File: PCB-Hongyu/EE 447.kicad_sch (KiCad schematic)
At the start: 9 parts, among them J1 Conn_01x04_Pin, U1 TSC2046IPWR

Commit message: file
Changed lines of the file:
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@@
 	)
 	(sheet
-		(at 203.2 26.67)
-		(size 22.86 29.21)
+		(at 217.17 26.67)
+		(size 20.32 21.59)
 		(exclude_from_sim no)
 		(in_bom yes)
@@
 		)
 		(property "Sheetname" "Epaper"
-			(at 203.2 25.9584 0)
+			(at 217.17 25.9584 0)
 			(effects
 				(font
@@
 		)
 		(property "Sheetfile" "../PCB_June/PCB.kicad_sch"
-			(at 203.2 56.4646 0)
+			(at 217.17 48.8446 0)
 			(effects
 				(font

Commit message: yur
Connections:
- net EPD_DC: now reaches U2.25 (IO5)
- net EPD_RST: now reaches U2.26 (IO4)
- net EPD_BUSY: now reaches U2.28 (IO18)
- net EPD_CS: now reaches U2.5 (IO3)
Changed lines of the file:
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@@
+	(wire
+		(pts
+			(xy 154.94 83.82) (xy 161.29 83.82)
+		)
+		(stroke
+			(width 0)
+			(type default)
+		)
+	)
 	(wire
 		(pts
@@
 	(wire
 		(pts
+			(xy 154.94 78.74) (xy 161.29 78.74)
+		)
+		(stroke
+			(width 0)
+			(type default)
+		)
+	)
+	(wire
+		(pts
 			(xy 80.01 95.25) (xy 80.01 96.52)
 		)
@@
 	(wire
 		(pts
+			(xy 124.46 63.5) (xy 130.81 63.5)
+		)
+		(stroke
+			(width 0)
+			(type default)
+		)
+	)
+	(wire
+		(pts
 			(xy 77.47 119.38) (xy 77.47 110.49)
 		)
@@
 		(pts
 			(xy 77.47 110.49) (xy 110.49 110.49)
+		)
+		(stroke
+			(width 0)
+			(type default)
+		)
+	)
+	(wire
+		(pts
+			(xy 154.94 76.2) (xy 161.29 76.2)
 		)
 		(stroke
@@
 		)
 	)
+	(global_label "EPD_DC"
+		(shape output)
+		(at 161.29 76.2 0)
+		(fields_autoplaced yes)
+		(effects
+			(font
+				(size 1.27 1.27)
+			)
+			(justify left)
+		)
+		(property "Intersheetrefs" "${INTERSHEET_REFS}"
+			(at 171.4718 76.2 0)
+			(effects
+				(font
+					(size 1.27 1.27)
+				)
+				(justify left)
+				(hide yes)
+			)
+		)
+	)
 	(global_label "CLK"
 		(shape input)
@@
 		)
 	)
+	(global_label "EPD_CS"
+		(shape output)
+		(at 124.46 63.5 180)
+		(fields_autoplaced yes)
+		(effects
+			(font
+				(size 1.27 1.27)
+			)
+			(justify right)
+		)
+		(property "Intersheetrefs" "${INTERSHEET_REFS}"
+			(at 114.3387 63.5 0)
+			(effects
+				(font
+					(size 1.27 1.27)
+				)
+				(justify right)
+				(hide yes)
+			)
+		)
+	)
 	(global_label "CS_TSC"
 		(shape input)
@@
 			(effects
 				(font
+					(size 1.27 1.27)
+				)
+				(justify left)
+				(hide yes)
+			)
+		)
+	)
+	(global_label "EPD_RST"
+		(shape output)
+		(at 161.29 78.74 0)
+		(fields_autoplaced yes)
+		(effects
+			(font
+				(size 1.27 1.27)
+			)
+			(justify left)
+		)
+		(property "Intersheetrefs" "${INTERSHEET_REFS}"
+			(at 172.3789 78.74 0)
+			(effects
+				(font
+					(size 1.27 1.27)
+				)
+				(justify left)
+				(hide yes)
+			)
+		)
+	)
+	(global_label "EPD_BUSY"
+		(shape output)
+		(at 161.29 83.82 0)
+		(fields_autoplaced yes)
+		(effects
+			(font
+				(size 1.27 1.27)
+			)
+			(justify left)
+		)
+		(property "Intersheetrefs" "${INTERSHEET_REFS}"
+			(at 173.8304 83.82 0)
+			(effects
+				(font

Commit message: MCB
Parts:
- added H1, H2, H3: MountingHole, MountingHole:MountingHole_3.2mm_M3, symbol Mechanical:MountingHole
- C1, C2, C3, C5: value ~ -> NC
- C4: value 10 uF -> 10u
- C6: value 0.1 uF -> 0.1u
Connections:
- net PENIRQ: now reaches U2.20 (IO9)
- net PENIRQ: now also U1.11 (*PENIRQ)
- no-connect marks 2 -> 8

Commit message: added power digikey links
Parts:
- C1, C2, C3, C5: now not fitted
- C4: Part Number (none) -> GRM21BR61H106KE43L
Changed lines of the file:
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@@
 			)
 		)
-		(property "Datasheet" "~"
+		(property "Datasheet" "https://www.digikey.com/en/products/detail/murata-electronics/GRM21BR61H106KE43L/10326316"
 			(at 80.01 91.44 0)
 			(effects
@@
 			)
 		)
+		(property "Part Number" "GRM21BR61H106KE43L"
+			(at 80.01 91.44 0)
+			(effects
+				(font
+					(size 1.27 1.27)
+				)
+				(hide yes)
+			)
+		)
 		(pin "1"
 		)
@@
 		(in_bom yes)
 		(on_board yes)
-		(dnp no)
+		(dnp yes)
 		(fields_autoplaced yes)
 		(property "Reference" "C2"
@@
 		(in_bom yes)
 		(on_board yes)
-		(dnp no)
+		(dnp yes)
 		(fields_autoplaced yes)
 		(property "Reference" "C3"
@@
 		(in_bom yes)
 		(on_board yes)
-		(dnp no)
+		(dnp yes)
 		(fields_autoplaced yes)
 		(property "Reference" "C5"
@@
 		(in_bom yes)
 		(on_board yes)
-		(dnp no)
+		(dnp yes)
 		(fields_autoplaced yes)
 		(property "Reference" "C1"

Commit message: added some stuff
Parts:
- C1, C2, C3, C5: footprint Capacitor_SMD:C_0805_2012Metric_Pad1.18x1.45mm_HandSolder -> Capacitor_SMD:C_0603_1608Metric_Pad1.08x0.95mm_HandSolder; now fitted
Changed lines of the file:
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@@
 		(in_bom yes)
 		(on_board yes)
-		(dnp yes)
+		(dnp no)
 		(fields_autoplaced yes)
 		(property "Reference" "C2"
@@
 			)
 		)
-		(property "Footprint" "Capacitor_SMD:C_0805_2012Metric_Pad1.18x1.45mm_HandSolder"
+		(property "Footprint" "Capacitor_SMD:C_0603_1608Metric_Pad1.08x0.95mm_HandSolder"
 			(at 65.7352 127 0)
 			(effects
@@
 			)
 		)
-		(property "Datasheet" "~"
+		(property "Datasheet" "https://www.digikey.com/en/products/detail/samsung-electro-mechanics/CL21B104KBCNNNC/3886661"
 			(at 93.98 91.44 0)
 			(effects
@@
 		(in_bom yes)
 		(on_board yes)
-		(dnp yes)
+		(dnp no)
 		(fields_autoplaced yes)
 		(property "Reference" "C3"
@@
 			)
 		)
-		(property "Footprint" "Capacitor_SMD:C_0805_2012Metric_Pad1.18x1.45mm_HandSolder"
+		(property "Footprint" "Capacitor_SMD:C_0603_1608Metric_Pad1.08x0.95mm_HandSolder"
 			(at 78.4352 127 0)
 			(effects
@@
 		(in_bom yes)
 		(on_board yes)
-		(dnp yes)
+		(dnp no)
 		(fields_autoplaced yes)
 		(property "Reference" "C5"
@@
 			)
 		)
-		(property "Footprint" "Capacitor_SMD:C_0805_2012Metric_Pad1.18x1.45mm_HandSolder"
+		(property "Footprint" "Capacitor_SMD:C_0603_1608Metric_Pad1.08x0.95mm_HandSolder"
 			(at 91.1352 127 0)
 			(effects
@@
 		(in_bom yes)
 		(on_board yes)
-		(dnp yes)
+		(dnp no)
 		(fields_autoplaced yes)
 		(property "Reference" "C1"
@@
 			)
 		)
-		(property "Footprint" "Capacitor_SMD:C_0805_2012Metric_Pad1.18x1.45mm_HandSolder"
+		(property "Footprint" "Capacitor_SMD:C_0603_1608Metric_Pad1.08x0.95mm_HandSolder"
 			(at 53.0352 127 0)
 			(effects

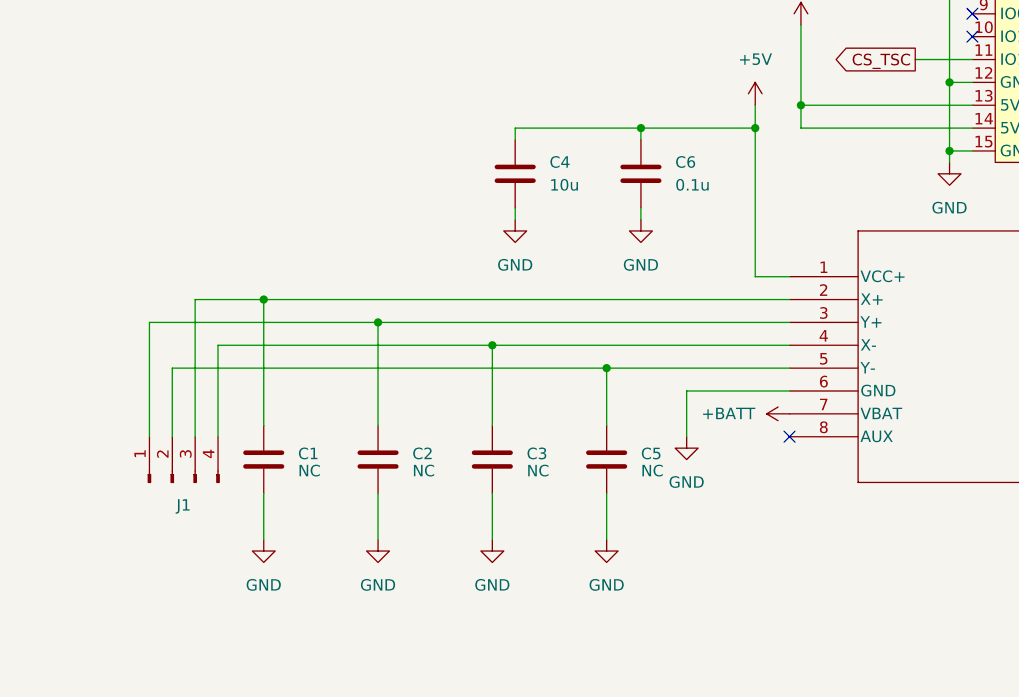
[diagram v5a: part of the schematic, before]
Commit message: finished adding parts and fixing silkscreen
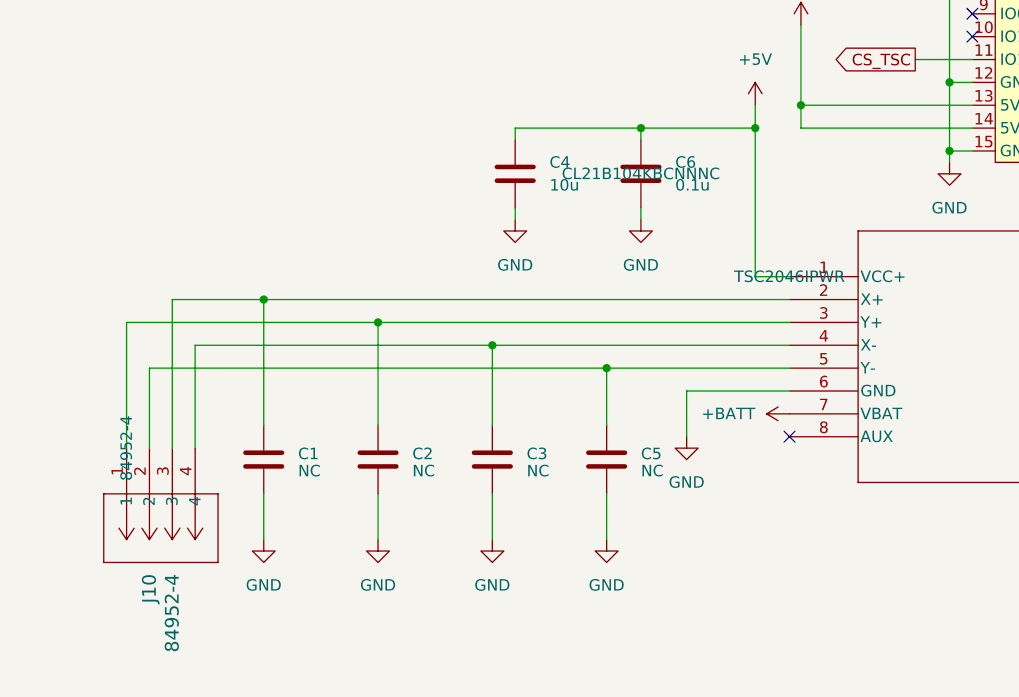
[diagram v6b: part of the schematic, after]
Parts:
- removed J1: Conn_01x04_Pin, Connector_FFC-FPC:JUSHUO_AFA07-S04FCA-00_1x4-1MP_P1.0mm_Horizontal, symbol Connector:Conn_01x04_Pin
- added J10: 84952-4, Hongyu:CON4_SMT-RA_FCC-FPC2, symbol 2025-04-15_05-15-59:84952-4
- C6: Part Number (none) -> CL21B104KBCNNNC
- U1: Part Number (none) -> TSC2046IPWR
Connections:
- net at C2.1, U1.3 (Y+): now also J10.1
- net at C5.1, U1.5 (Y-): now also J10.2
- net at C1.1, U1.2 (X+): now also J10.3
- net at C3.1, U1.4 (X-): now also J10.4
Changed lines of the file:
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@@
 	(wire
 		(pts
-			(xy 44.45 105.41) (xy 44.45 120.65)
+			(xy 39.37 113.03) (xy 39.37 121.92)
 		)
 		(stroke
@@
 	(wire
 		(pts
-			(xy 46.99 110.49) (xy 77.47 110.49)
+			(xy 44.45 110.49) (xy 77.47 110.49)
 		)
 		(stroke
@@
 	(wire
 		(pts
-			(xy 39.37 107.95) (xy 39.37 120.65)
-		)
-		(stroke
-			(width 0)
-			(type default)
-		)
-	)
-	(wire
-		(pts
 			(xy 111.76 83.82) (xy 130.81 83.82)
 		)
@@
 	(wire
 		(pts
-			(xy 44.45 105.41) (xy 52.07 105.41)
-		)
-		(stroke
-			(width 0)
-			(type default)
-		)
-	)
-	(wire
-		(pts
-			(xy 41.91 113.03) (xy 90.17 113.03)
-		)
-		(stroke
-			(width 0)
-			(type default)
-		)
-	)
-	(wire
-		(pts
-			(xy 41.91 113.03) (xy 41.91 120.65)
+			(xy 41.91 105.41) (xy 52.07 105.41)
+		)
+		(stroke
+			(width 0)
+			(type default)
+		)
+	)
+	(wire
+		(pts
+			(xy 39.37 113.03) (xy 90.17 113.03)
 		)
 		(stroke
@@
 	(wire
 		(pts
-			(xy 46.99 110.49) (xy 46.99 120.65)
-		)
-		(stroke
-			(width 0)
-			(type default)
-		)
-	)
-	(wire
-		(pts
 			(xy 90.17 113.03) (xy 110.49 113.03)
 		)
@@
 	(wire
 		(pts
-			(xy 39.37 107.95) (xy 64.77 107.95)
+			(xy 36.83 107.95) (xy 64.77 107.95)
 		)
 		(stroke
@@
 	(wire
 		(pts
+			(xy 41.91 105.41) (xy 41.91 121.92)
+		)
+		(stroke
+			(width 0)
+			(type default)
+		)
+	)
+	(wire
+		(pts
 			(xy 106.68 83.82) (xy 106.68 86.36)
 		)
@@
 	(wire
 		(pts
+			(xy 44.45 110.49) (xy 44.45 121.92)
+		)
+		(stroke
+			(width 0)
+			(type default)
+		)
+	)
+	(wire
+		(pts
 			(xy 163.83 58.42) (xy 163.83 55.88)
 		)
@@
 		(pts
 			(xy 128.27 71.12) (xy 128.27 81.28)
+		)
+		(stroke
+			(width 0)
+			(type default)
+		)
+	)
+	(wire
+		(pts
+			(xy 36.83 107.95) (xy 36.83 121.92)
 		)
 		(stroke
@@
 	)
 	(symbol
+		(lib_id "2025-04-15_05-15-59:84952-4")
+		(at 36.83 121.92 90)
+		(mirror x)
+		(unit 1)
+		(exclude_from_sim no)
+		(in_bom yes)
+		(on_board yes)
+		(dnp no)
+		(property "Reference" "J10"
+			(at 39.3699 135.89 0)
+			(effects
+				(font
+					(size 1.524 1.524)
+				)
+				(justify left)
+			)
+		)
+		(property "Value" "84952-4"
+			(at 41.9099 135.89 0)
+			(effects
+				(font
+					(size 1.524 1.524)
+				)
+				(justify left)
+			)
+		)
+		(property "Footprint" "Hongyu:CON4_SMT-RA_FCC-FPC2"
+			(at 36.83 121.92 0)
+			(effects
+				(font
+					(size 1.27 1.27)
+					(italic yes)
+				)
+				(hide yes)
+			)
+		)
+		(property "Datasheet" "https://www.digikey.com/en/products/detail/te-connectivity-amp-connectors/84952-4/2056112"
+			(at 36.83 121.92 0)
+			(effects
+				(font
+					(size 1.27 1.27)
+					(italic yes)
+				)
+				(hide yes)
+			)
+		)
+		(property "Description" ""
+			(at 36.83 121.92 0)
+			(effects
+				(font
+					(size 1.27 1.27)
+				)
+				(hide yes)
+			)
+		)
+		(property "Part Number" "84952-4"
+			(at 36.83 121.92 0)
+			(effects
+				(font
+					(size 1.27 1.27)
+				)
+			)
+		)
+		(pin "3"
+		)
+		(pin "1"
+		)
+		(pin "2"
+		)
+		(pin "4"
+		)
+		(instances
+			(project ""
+				(path "/8dcae476-bf02-4dea-8567-670805b7ab7c"
+					(reference "J10")
+					(unit 1)
+				)
+			)
+		)
+	)
+	(symbol
 		(lib_id "power:+BATT")
 		(at 111.76 74.93 0)
@@
 	)
 	(symbol
-		(lib_id "Connector:Conn_01x04_Pin")
-		(at 41.91 125.73 90)
-		(unit 1)
-		(exclude_from_sim no)
-		(in_bom yes)
-		(on_board yes)
-		(dnp no)
-		(fields_autoplaced yes)
-		(property "Reference" "J1"
-			(at 43.18 128.27 90)
-			(effects
-				(font
-					(size 1.27 1.27)
-				)
-			)
-		)
-		(property "Value" "Conn_01x04_Pin"
-			(at 43.18 130.81 90)
-			(effects
-				(font
-					(size 1.27 1.27)
-				)
-				(hide yes)
-			)
-		)
-		(property "Footprint" "Connector_FFC-FPC:JUSHUO_AFA07-S04FCA-00_1x4-1MP_P1.0mm_Horizontal"
-			(at 41.91 125.73 0)
-			(effects
-				(font
-					(size 1.27 1.27)
-				)
-				(hide yes)
-			)
-		)
-		(property "Datasheet" "~"
-			(at 41.91 125.73 0)
-			(effects
-				(font
-					(size 1.27 1.27)
-				)
-				(hide yes)
-			)
-		)
-		(property "Description" "Generic connector, single row, 01x04, script generated"
-			(at 41.91 125.73 0)
-			(effects
-				(font
-					(size 1.27 1.27)
-				)
-				(hide yes)
-			)
-		)
-		(pin "2"
-		)
-		(pin "3"
-		)
-		(pin "1"
-		)
-		(pin "4"
-		)
-		(instances
-			(project ""
-				(path "/8dcae476-bf02-4dea-8567-670805b7ab7c"
-					(reference "J1")
-					(unit 1)
-				)
-			)
-		)
-	)
-	(symbol
 		(lib_id "power:+5V")
 		(at 106.68 83.82 0)
@@
 			)
 		)
+		(property "Part Number" "CL21B104KBCNNNC"
+			(at 93.98 91.44 0)
+			(effects
+				(font
+					(size 1.27 1.27)
+				)
+			)
+		)
 		(pin "1"
 		)
@@
 			)
 		)
-		(property "Datasheet" "TSC2046IPWR"
+		(property "Datasheet" "https://www.digikey.com/en/products/detail/texas-instruments/TSC2046IPWR/562831"
 			(at 110.49 102.87 0)
 			(effects
@@
 			)
 		)
+		(property "Part Number" "TSC2046IPWR"
+			(at 110.49 102.87 0)
+			(effects
+				(font
+					(size 1.27 1.27)
+				)
+			)
+		)

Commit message: small fixes
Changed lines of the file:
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@@
 					(size 1.27 1.27)
 				)
+				(hide yes)
 			)
 		)
@@
 					(size 1.27 1.27)
 				)
+				(hide yes)
 			)
 		)
@@
 					(size 1.27 1.27)
 				)
-			)
-		)
+				(hide yes)
+			)
+		)

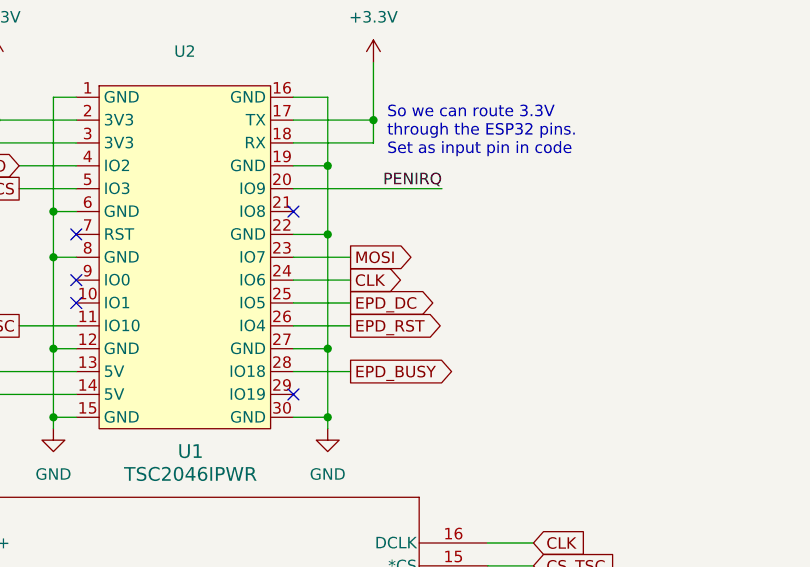
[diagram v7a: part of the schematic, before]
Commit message: penirq change pin
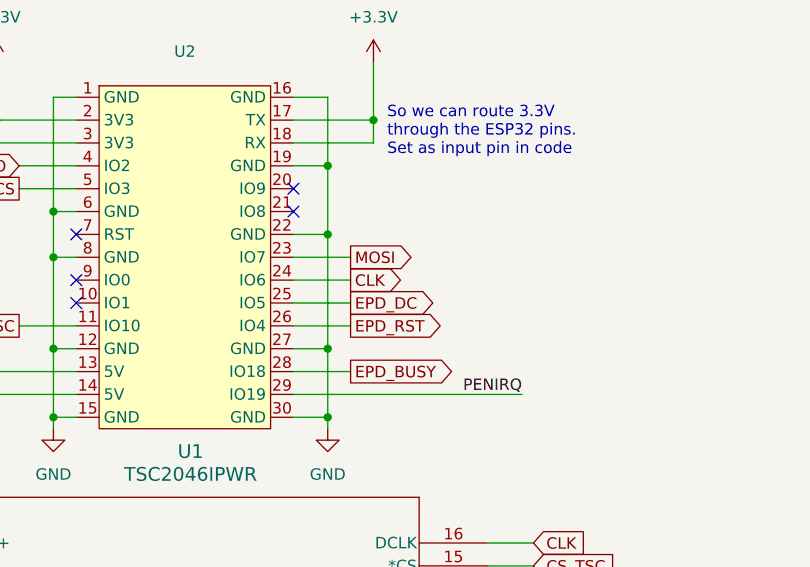
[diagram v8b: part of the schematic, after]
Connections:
- net PENIRQ: now also U2.29 (IO19); no longer U2.20 (IO9)
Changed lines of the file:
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@@
-	)
-	(no_connect
-		(at 154.94 86.36)
 	)
 	(no_connect
@@
 	)
 	(no_connect
+		(at 154.94 63.5)
+	)
+	(no_connect
 		(at 130.81 68.58)
 	)
@@
 	(wire
 		(pts
+			(xy 154.94 86.36) (xy 180.34 86.36)
+		)
+		(stroke
+			(width 0)
+			(type default)
+		)
+	)
+	(wire
+		(pts
 			(xy 154.94 55.88) (xy 163.83 55.88)
 		)
@@
 	(wire
 		(pts
-			(xy 154.94 63.5) (xy 171.45 63.5)
-		)
-		(stroke
-			(width 0)
-			(type default)
-		)
-	)
-	(wire
-		(pts
 			(xy 110.49 115.57) (xy 99.06 115.57)
 		)
@@
 	)
 	(label "PENIRQ"
-		(at 181.61 115.57 180)
+		(at 180.34 86.36 180)
 		(effects
 			(font
@@
 	)
 	(label "PENIRQ"
-		(at 171.45 63.5 180)
+		(at 181.61 115.57 180)
 		(effects
 			(font
